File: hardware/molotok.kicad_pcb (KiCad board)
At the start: 2 copper layers, 37 x 23 mm, 16 parts, among them J1 Power, J2 LED, Q1 Q_PMOS_GSD, Q2 DMG9926UDM, SW1 SW_Push, U1 ATtiny85-20SU, U2 AP9101C-SOT-25

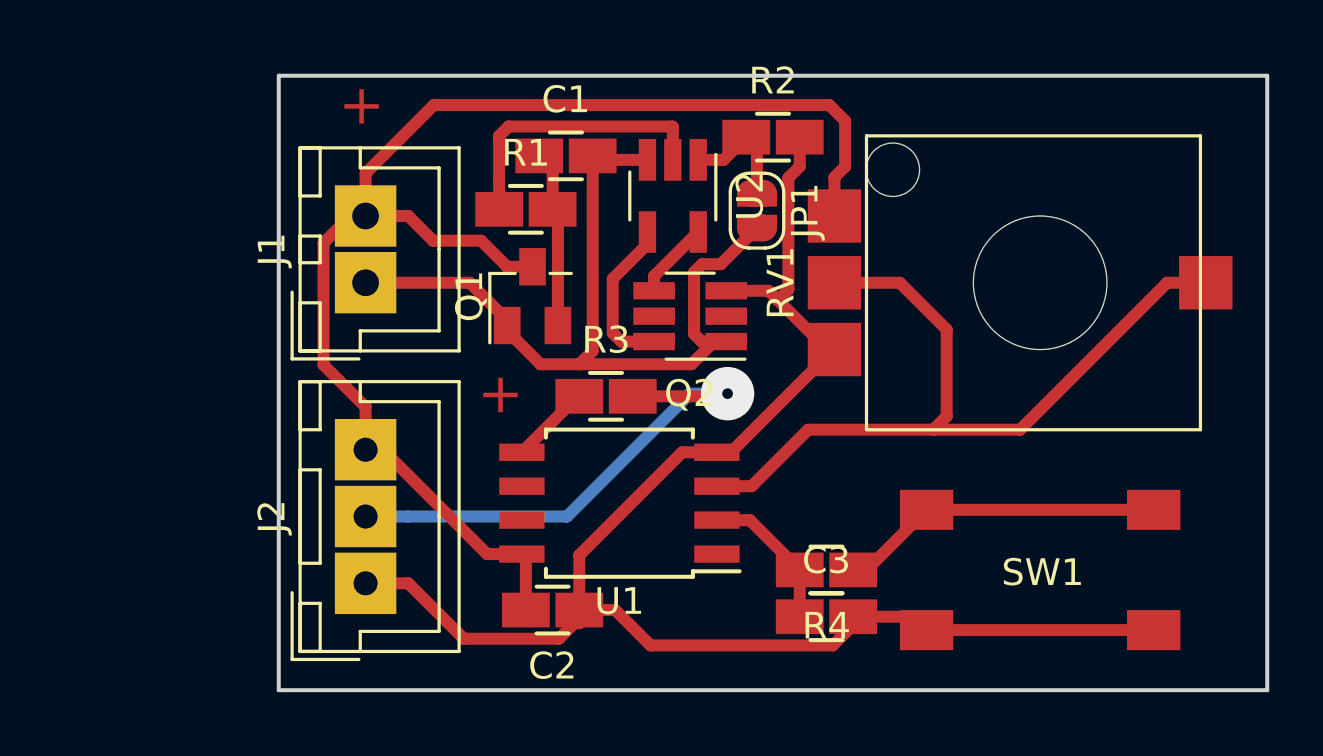
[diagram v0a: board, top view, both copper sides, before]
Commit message: Reversing mosfet orientation to be correct.
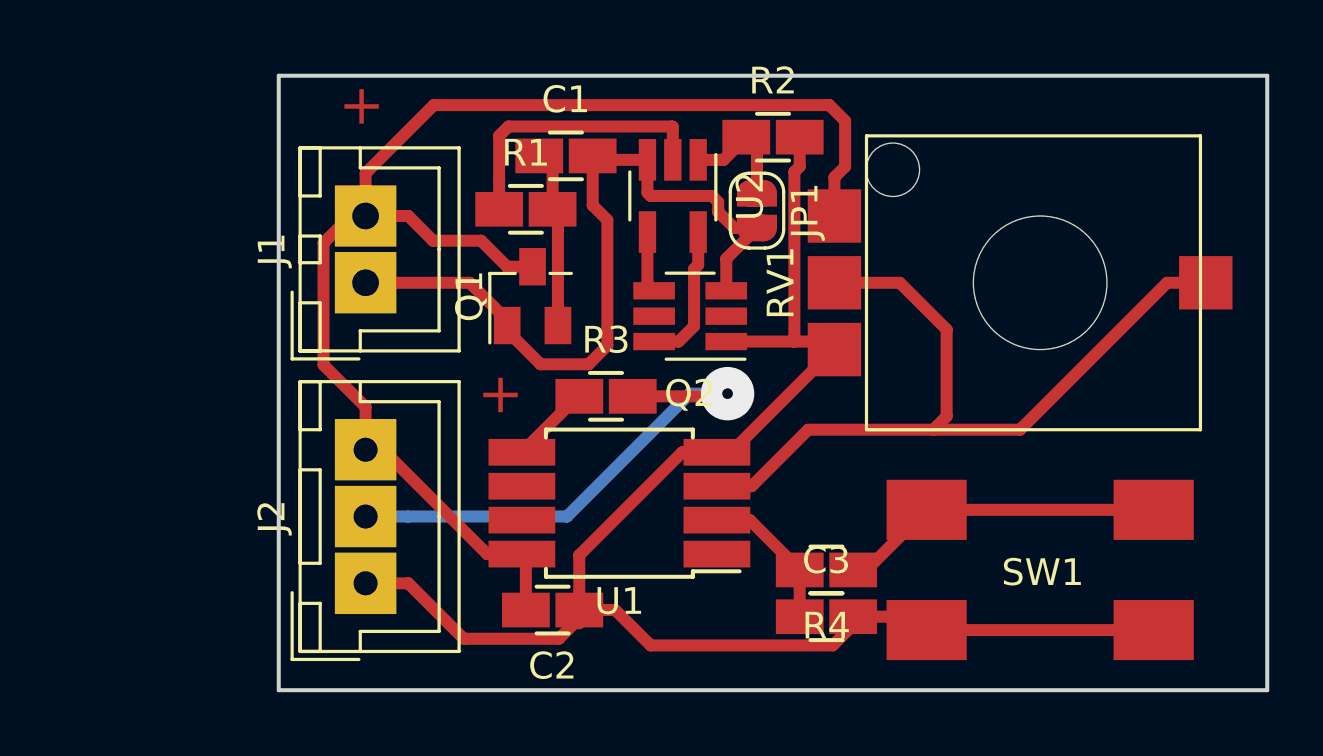
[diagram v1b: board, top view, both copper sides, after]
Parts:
- JP1: value Jumper_NO_Small -> Dis Curr Limit
- SW1: value SW_Push -> Control
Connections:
- Q2 pad 1: Net-(C1-Pad2) -> GND
- Q2 pad 3: GND -> Net-(C1-Pad2)
- U2 pad 4: Net-(Q2-Pad6) -> Net-(Q2-Pad4)
- U2 pad 5: Net-(Q2-Pad4) -> Net-(Q2-Pad6)
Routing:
- net Net-(C1-Pad2): track 32.1 -> 29.2 mm
- net Net-(Q2-Pad6): track 6.00 -> 5.32 mm
- net Net-(Q2-Pad4): track 2.88 -> 2.30 mm
- net GND: track 59.1 -> 59.6 mm

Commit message: Use a rotary encoder instead of a potentiometer for control.
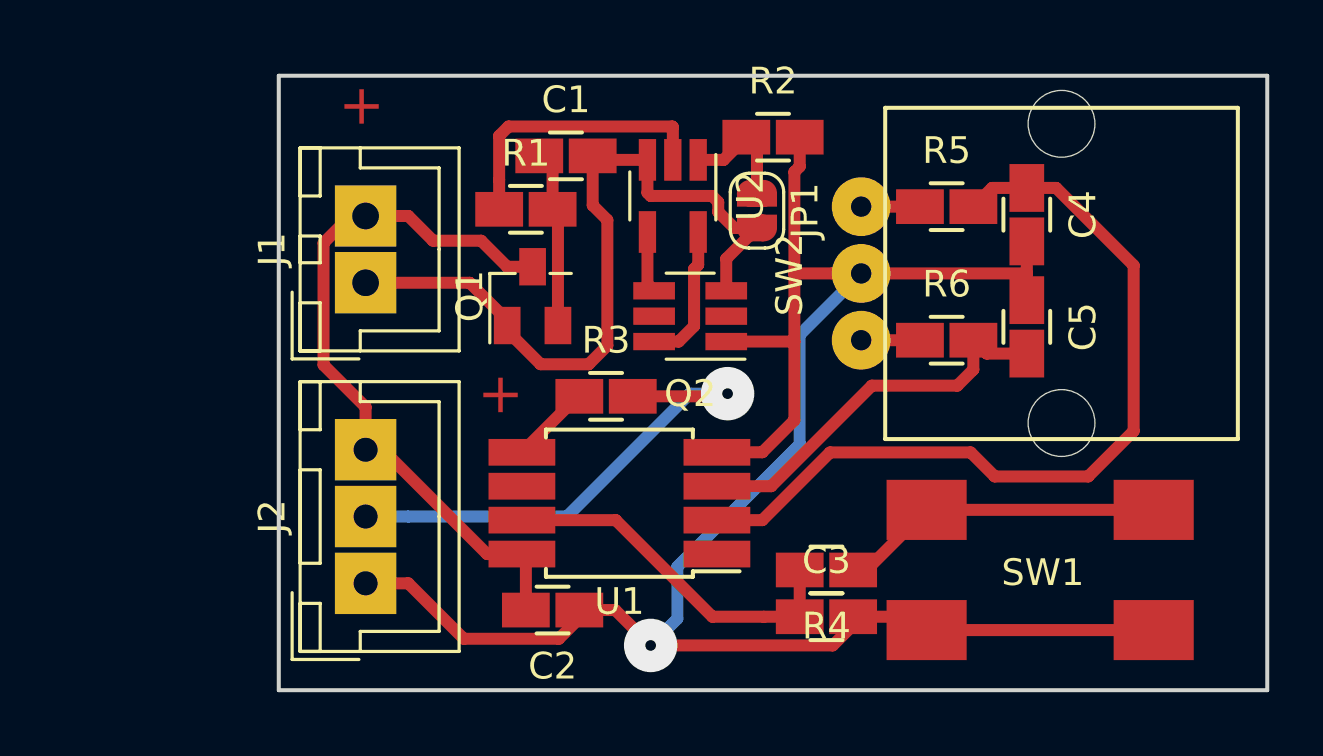
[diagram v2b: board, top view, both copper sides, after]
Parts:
- removed RV1: R_POT, coddingtonbear:SV01_Murata_Pot
- added C4: 0.1u, coddingtonbear:0805_Milling, F.Cu at (132.0, 79.2)
- added C5: 0.1u, coddingtonbear:0805_Milling, F.Cu at (132.0, 83.4)
- added R5: 1k, coddingtonbear:0805_Milling, F.Cu at (129.0, 78.9)
- added R6: 1k, coddingtonbear:0805_Milling, F.Cu at (129.0, 83.9)
- added SW2: Rotary_Encoder, coddingtonbear:PES12, F.Cu at (133.3, 81.4)
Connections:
- U1 pad 2: BTN -> ROT_A
- U1 pad 3: Net-(RV1-Pad2) -> ROT_B
- U1 pad 7: Net-(U1-Pad7) -> BTN
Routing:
- net ROT_A: track 0.00 -> 31.4 mm
- net Net-(RV1-Pad2): track 30.3 -> 0.00 mm
- net VCC: track 51.6 -> 27.0 mm
- net GND: track 59.6 -> 77.1 mm, vias 0 -> 1
- net ROT_B: track 0.00 -> 14.7 mm
- net BTN: track 5.62 -> 13.6 mm
- net Net-(R6-Pad1): track 0.00 -> 2.20 mm
- net Net-(R5-Pad1): track 0.00 -> 2.20 mm

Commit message: Adding fuse.
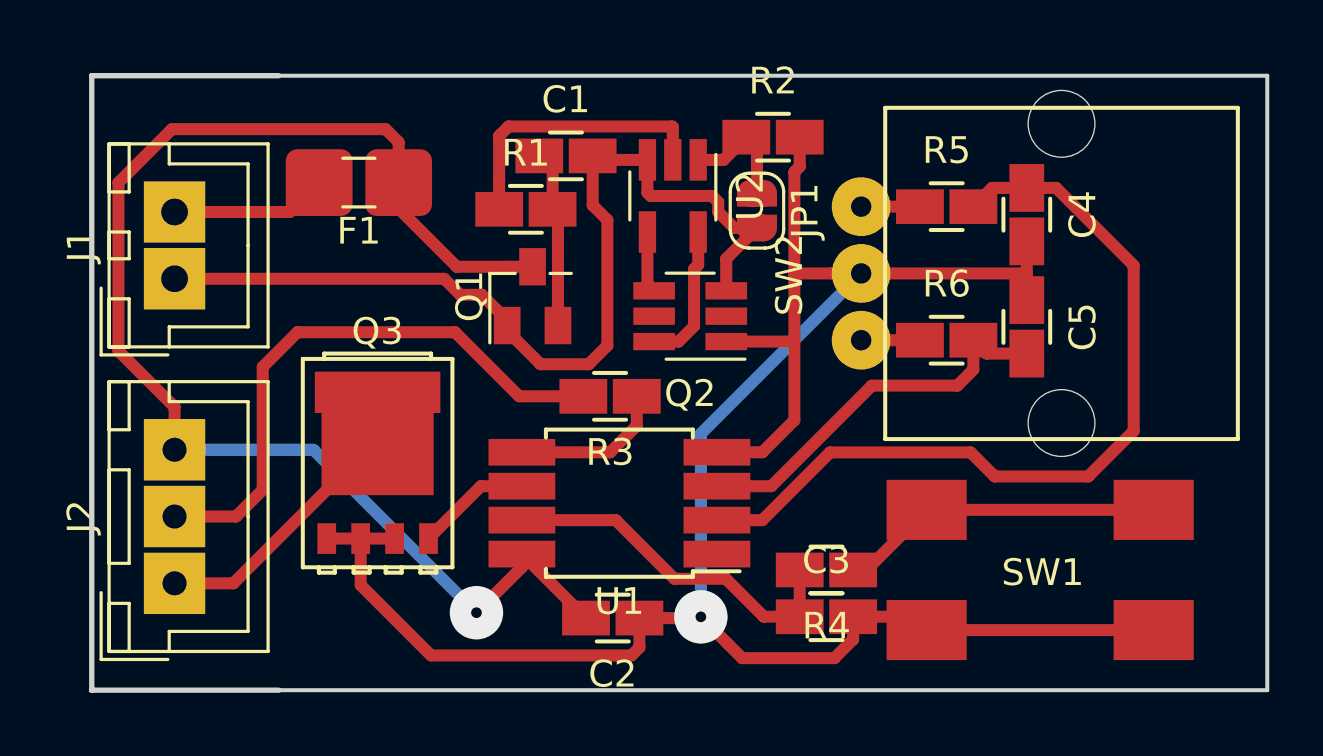
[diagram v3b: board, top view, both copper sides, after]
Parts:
- added F1: Fuse, coddingtonbear:R_1206_Fuse_HandSolder_LargePads, F.Cu at (107.0, 78.0)
- added Q3: Q_NMOS_SGD, coddingtonbear:PSMN5R4-25YLD, F.Cu at (107.7, 88.5)
- moved J1 7.15 mm to (100.1, 81.6)
- moved J2 7.15 mm to (100.1, 93.0)
- moved C2 2.27 mm to (116.5, 94.3)
- moved R3 0.15 mm to (116.4, 86.0), turned to 180 degrees
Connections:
- J1 pad 2: VCC -> Net-(F1-Pad2)
- J2 pad 1: GND -> Net-(J2-Pad1)
- U1 pad 6: Net-(U1-Pad6) -> ENABLE_NEOPIXEL
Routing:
- net VCC: track 27.0 -> 50.9 mm, vias 0 -> 1
- net Net-(J2-Pad1): track 0.00 -> 11.9 mm
- net Net-(C1-Pad2): track 29.2 -> 36.4 mm
- net Net-(F1-Pad2): track 0.00 -> 5.87 mm
- net ENABLE_NEOPIXEL: track 0.00 -> 4.31 mm
- net GND: track 77.1 -> 81.2 mm
- net Net-(J2-Pad2): track 19.0 -> 21.8 mm, vias 1 -> 0
- net NEOPIXEL: track 3.02 -> 5.81 mm
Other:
- board size 37 x 23 mm -> 44 x 23 mm
- board text removed: "+"
